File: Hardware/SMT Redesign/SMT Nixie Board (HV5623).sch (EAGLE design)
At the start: 43 parts, among them J4 1, T0 IN-14(R), T1 IN-14(R), T2 IN-14(R), T3 IN-14(R), T4 IN-14(R), T5 IN-14(R), T6 IN-14(R), T7 IN-14(R), U6 HV5623K7-G, U7 HV5623K7-G, U8 HV5623K7-G

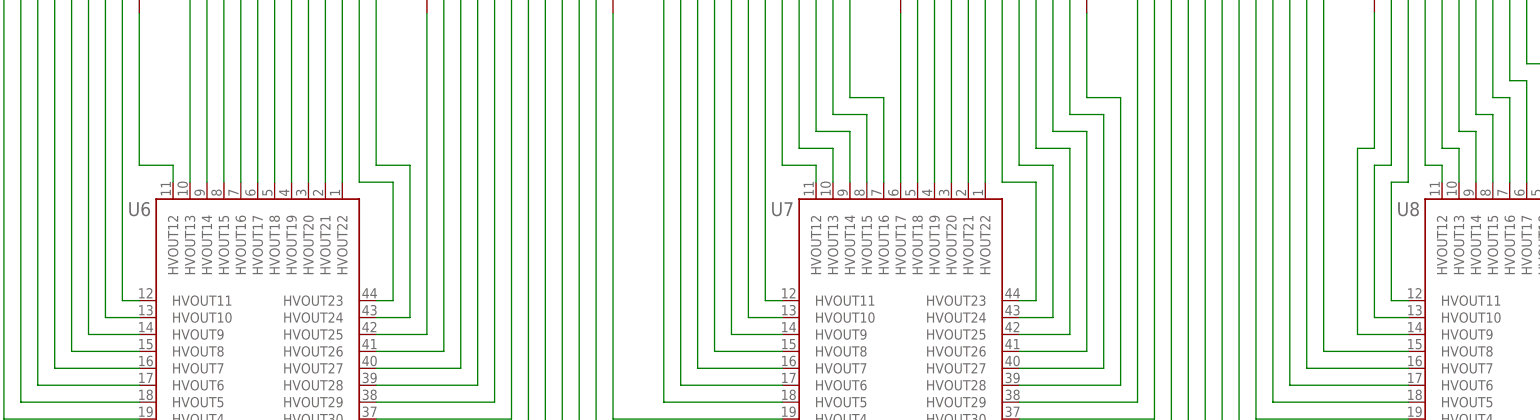
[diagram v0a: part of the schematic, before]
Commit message: Component numbering fix
There was a gap from U3 to U5, shifted U5 onwards down one (eg to U4).

Was also playing the with DR for JLCPCB, some pads etc may be wonky because of this.
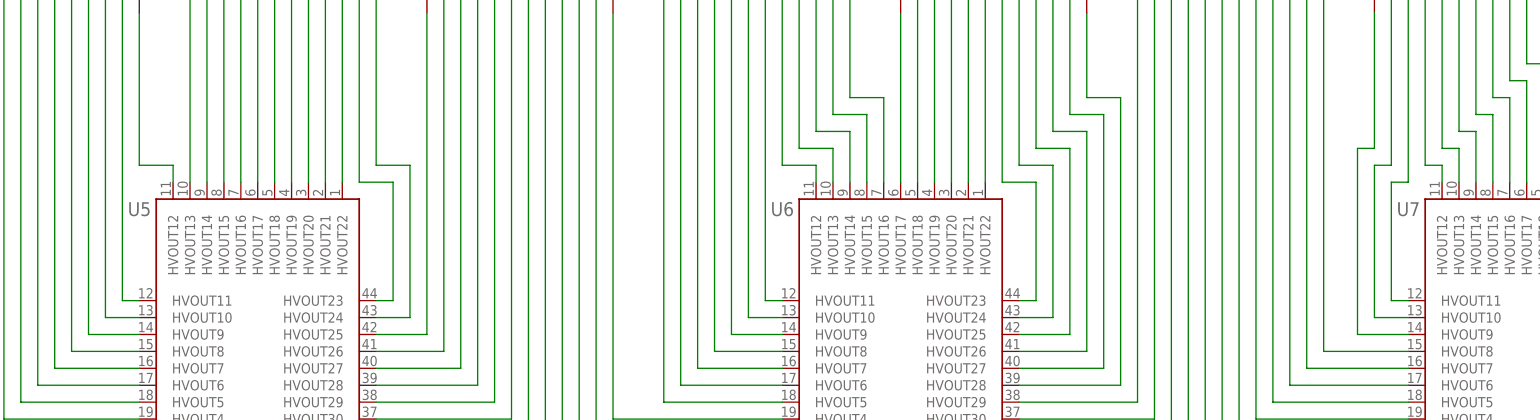
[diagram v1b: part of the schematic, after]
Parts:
- removed U8: HV5623K7-G, My Imported Components:HV5623K7-G
- added U5: HV5623K7-G, My Imported Components:HV5623K7-G
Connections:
- net !BL!: now also U5.!BL; no longer U8.!BL
- net !LE!: now also U5.!LE; no longer U8.!LE
- net +5V: now also U5.!POL, U5.VDD; no longer U8.!POL, U8.VDD
- net CLK: now also U5.CLK; no longer U8.CLK
- net DIN: now also U5.DATAIN; no longer U6.DATAIN
- net GND: now also U5.VSS; no longer U8.VSS
- net U5-T0K0: now also U5.HVOUT2; no longer U6.HVOUT2
- net U5-T0K1: now also U5.HVOUT11; no longer U6.HVOUT11
- net U5-T0K2: now also U5.HVOUT10; no longer U6.HVOUT10
- net U5-T0K3: now also U5.HVOUT9; no longer U6.HVOUT9
- net U5-T0K4: now also U5.HVOUT8; no longer U6.HVOUT8
- net U5-T0K5: now also U5.HVOUT7; no longer U6.HVOUT7
- net U5-T0K6: now also U5.HVOUT6; no longer U6.HVOUT6
- net U5-T0K7: now also U5.HVOUT5; no longer U6.HVOUT5
- net U5-T0K8: now also U5.HVOUT4; no longer U6.HVOUT4
- net U5-T0K9: now also U5.HVOUT3; no longer U6.HVOUT3
- net U5-T0LDP: now also U5.HVOUT12; no longer U6.HVOUT12
- net U5-T0RDP: now also U5.HVOUT1; no longer U6.HVOUT1
- net U5-T1K0: now also U5.HVOUT14; no longer U6.HVOUT14
- net U5-T1K1: now also U5.HVOUT23; no longer U6.HVOUT23
- net U5-T1K2: now also U5.HVOUT22; no longer U6.HVOUT22
- net U5-T1K3: now also U5.HVOUT21; no longer U6.HVOUT21
- net U5-T1K4: now also U5.HVOUT20; no longer U6.HVOUT20
- net U5-T1K5: now also U5.HVOUT19; no longer U6.HVOUT19
- net U5-T1K6: now also U5.HVOUT18; no longer U6.HVOUT18
- net U5-T1K7: now also U5.HVOUT17; no longer U6.HVOUT17
- net U5-T1K8: now also U5.HVOUT16; no longer U6.HVOUT16
- net U5-T1K9: now also U5.HVOUT15; no longer U6.HVOUT15
- net U5-T1LDP: now also U5.HVOUT24; no longer U6.HVOUT24
- net U5-T1RDP: now also U5.HVOUT13; no longer U6.HVOUT13
- net U5-T2K0: now also U5.HVOUT26; no longer U6.HVOUT26
- net U5-T2K4: now also U5.HVOUT32; no longer U6.HVOUT32
- net U5-T2K5: now also U5.HVOUT31; no longer U6.HVOUT31
- net U5-T2K6: now also U5.HVOUT30; no longer U6.HVOUT30
- net U5-T2K7: now also U5.HVOUT29; no longer U6.HVOUT29
- net U5-T2K8: now also U5.HVOUT28; no longer U6.HVOUT28
- net U5-T2K9: now also U5.HVOUT27; no longer U6.HVOUT27
- net U5-T2RDP: now also U5.HVOUT25; no longer U6.HVOUT25
- net U5-U6: now also U5.DATAOUT, U6.DATAIN; no longer U6.DATAOUT, U7.DATAIN
- net U6-T2K1: now also U6.HVOUT3; no longer U7.HVOUT3
- net U6-T2K2: now also U6.HVOUT2; no longer U7.HVOUT2
- net U6-T2K3: now also U6.HVOUT1; no longer U7.HVOUT1
- net U6-T2LDP: now also U6.HVOUT4; no longer U7.HVOUT4
- net U6-T3K0: now also U6.HVOUT6; no longer U7.HVOUT6
- net U6-T3K1: now also U6.HVOUT15; no longer U7.HVOUT15
- net U6-T3K2: now also U6.HVOUT14; no longer U7.HVOUT14
- net U6-T3K3: now also U6.HVOUT13; no longer U7.HVOUT13
- net U6-T3K4: now also U6.HVOUT12; no longer U7.HVOUT12
- net U6-T3K5: now also U6.HVOUT11; no longer U7.HVOUT11
- net U6-T3K6: now also U6.HVOUT10; no longer U7.HVOUT10
- net U6-T3K7: now also U6.HVOUT9; no longer U7.HVOUT9
- net U6-T3K8: now also U6.HVOUT8; no longer U7.HVOUT8
- net U6-T3K9: now also U6.HVOUT7; no longer U7.HVOUT7
- net U6-T3LDP: now also U6.HVOUT16; no longer U7.HVOUT16
- net U6-T3RDP: now also U6.HVOUT5; no longer U7.HVOUT5
- net U6-T4K0: now also U6.HVOUT18; no longer U7.HVOUT18
- net U6-T4K1: now also U6.HVOUT27; no longer U7.HVOUT27
- net U6-T4K2: now also U6.HVOUT26; no longer U7.HVOUT26
- net U6-T4K3: now also U6.HVOUT25; no longer U7.HVOUT25
- net U6-T4K4: now also U6.HVOUT24; no longer U7.HVOUT24
- net U6-T4K5: now also U6.HVOUT23; no longer U7.HVOUT23
- net U6-T4K6: now also U6.HVOUT22; no longer U7.HVOUT22
- net U6-T4K7: now also U6.HVOUT21; no longer U7.HVOUT21
- net U6-T4K8: now also U6.HVOUT20; no longer U7.HVOUT20
- net U6-T4K9: now also U6.HVOUT19; no longer U7.HVOUT19
- net U6-T4LDP: now also U6.HVOUT28; no longer U7.HVOUT28
- net U6-T4RDP: now also U6.HVOUT17; no longer U7.HVOUT17
- net U6-T5K0: now also U6.HVOUT30; no longer U7.HVOUT30
- net U6-T5K8: now also U6.HVOUT32; no longer U7.HVOUT32
- net U6-T5K9: now also U6.HVOUT31; no longer U7.HVOUT31
- net U6-T5RDP: now also U6.HVOUT29; no longer U7.HVOUT29
- net U6-U7: now also U6.DATAOUT, U7.DATAIN; no longer U7.DATAOUT, U8.DATAIN
- net U7-T5K1: now also U7.HVOUT7; no longer U8.HVOUT7
- net U7-T5K2: now also U7.HVOUT6; no longer U8.HVOUT6
- net U7-T5K3: now also U7.HVOUT5; no longer U8.HVOUT5
- net U7-T5K4: now also U7.HVOUT4; no longer U8.HVOUT4
- net U7-T5K5: now also U7.HVOUT3; no longer U8.HVOUT3
- net U7-T5K6: now also U7.HVOUT2; no longer U8.HVOUT2
- net U7-T5K7: now also U7.HVOUT1; no longer U8.HVOUT1
- net U7-T5LDP: now also U7.HVOUT8; no longer U8.HVOUT8
- net U7-T6K0: now also U7.HVOUT10; no longer U8.HVOUT10
- net U7-T6K1: now also U7.HVOUT19; no longer U8.HVOUT19
- net U7-T6K2: now also U7.HVOUT18; no longer U8.HVOUT18
- net U7-T6K3: now also U7.HVOUT17; no longer U8.HVOUT17
- net U7-T6K4: now also U7.HVOUT16; no longer U8.HVOUT16
- net U7-T6K5: now also U7.HVOUT15; no longer U8.HVOUT15
- net U7-T6K6: now also U7.HVOUT14; no longer U8.HVOUT14
- net U7-T6K7: now also U7.HVOUT13; no longer U8.HVOUT13
- net U7-T6K8: now also U7.HVOUT12; no longer U8.HVOUT12
- net U7-T6K9: now also U7.HVOUT11; no longer U8.HVOUT11
- net U7-T6LDP: now also U7.HVOUT20; no longer U8.HVOUT20
- net U7-T6RDP: now also U7.HVOUT9; no longer U8.HVOUT9
- net U7-T7K0: now also U7.HVOUT22; no longer U8.HVOUT22
- net U7-T7K1: now also U7.HVOUT31; no longer U8.HVOUT31
- net U7-T7K2: now also U7.HVOUT30; no longer U8.HVOUT30
- net U7-T7K3: now also U7.HVOUT29; no longer U8.HVOUT29
- net U7-T7K4: now also U7.HVOUT28; no longer U8.HVOUT28
- net U7-T7K5: now also U7.HVOUT27; no longer U8.HVOUT27
- net U7-T7K6: now also U7.HVOUT26; no longer U8.HVOUT26
- net U7-T7K7: now also U7.HVOUT25; no longer U8.HVOUT25
- net U7-T7K8: now also U7.HVOUT24; no longer U8.HVOUT24
- net U7-T7K9: now also U7.HVOUT23; no longer U8.HVOUT23
- net U7-T7LDP: now also U7.HVOUT32; no longer U8.HVOUT32
- net U7-T7RDP: now also U7.HVOUT21; no longer U8.HVOUT21
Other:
- moved on the sheet: U6, U7
